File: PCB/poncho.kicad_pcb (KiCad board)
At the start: 2 copper layers, 4 parts, among them P1 CONN_20X2, P2 CONN_20X2, P3 ESP8266

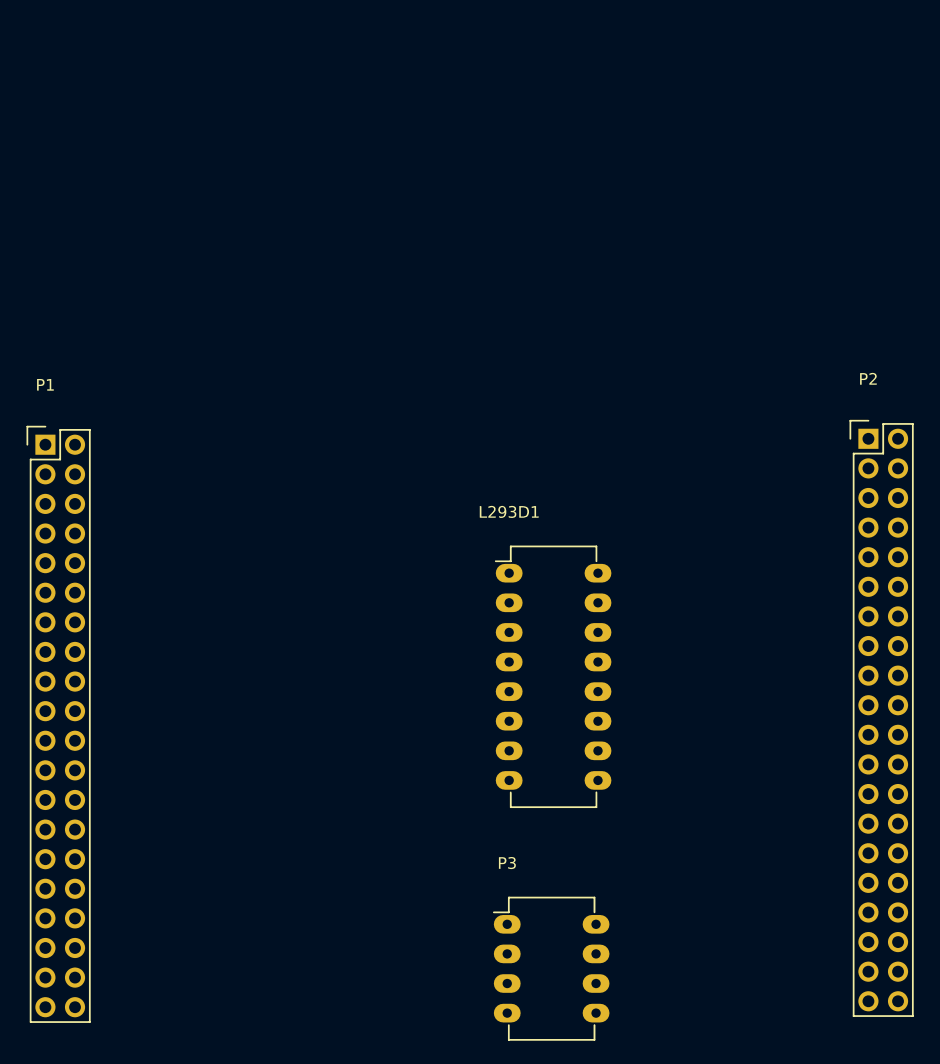
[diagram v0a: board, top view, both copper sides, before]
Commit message: Esquemático terminado. Poncho agregado. [TODO] Corregir eventuales errores. Chequear que estén bien.
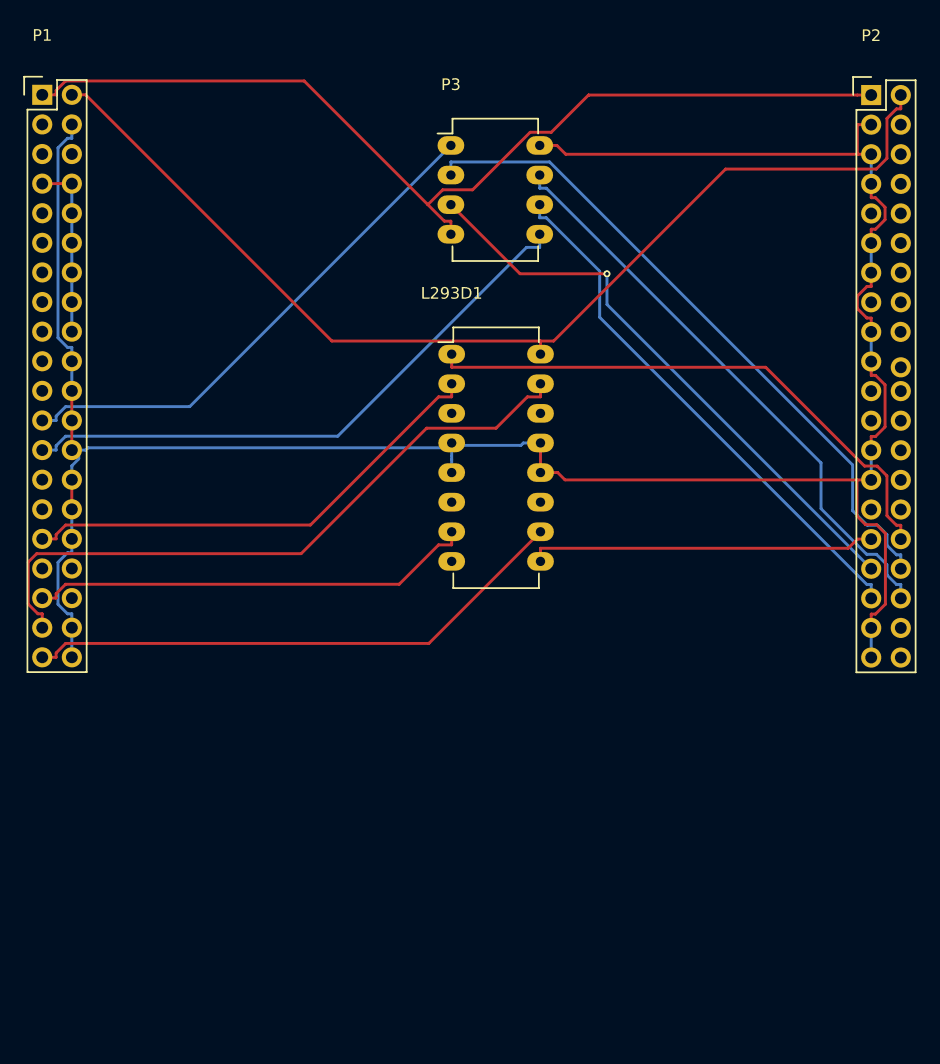
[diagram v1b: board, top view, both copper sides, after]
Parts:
- moved P3 67.0 mm to (143.5, 68.3)
- moved P1 30.0 mm to (108.4, 64.0)
- moved P2 29.5 mm to (179.6, 64.0)
- moved L293D1 19.4 mm to (143.6, 86.2)
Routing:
- net GND: track 0.00 -> 205.1 mm
- net +5V: track 0.00 -> 92.4 mm
- net +3V3: track 0.00 -> 83.8 mm
- net /GPIO3: track 0.00 -> 57.7 mm
- net /TEC_F2: track 0.00 -> 57.3 mm
- net /RS232_TXD: track 0.00 -> 51.2 mm
- net /GPIO4: track 0.00 -> 50.5 mm, vias 0 -> 1
- net /GPIO5: track 0.00 -> 50.2 mm
- net /GPIO1: track 0.00 -> 48.5 mm
- net /TEC_COL0: track 0.00 -> 47.4 mm
- net /GPIO6: track 0.00 -> 46.1 mm
- net /RS232_RXD: track 0.00 -> 45.1 mm
- net /TEC_COL1: track 0.00 -> 41.5 mm
- net /TEC_F3: track 0.00 -> 38.4 mm
- net /GPIO2: track 0.00 -> 29.8 mm
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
